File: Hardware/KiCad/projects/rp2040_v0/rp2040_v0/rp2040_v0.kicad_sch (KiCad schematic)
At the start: 52 parts, among them J1 Conn_01x03, J11 Conn_01x02, J12 Screw_Terminal_01x02, J2 Conn_01x02, J3 Conn_01x03, J5 USB_B_Micro, J8 Conn_01x03, J9 Conn_01x02, U1 W25Q128JVSIQTR, U2 AMS1117-3.3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

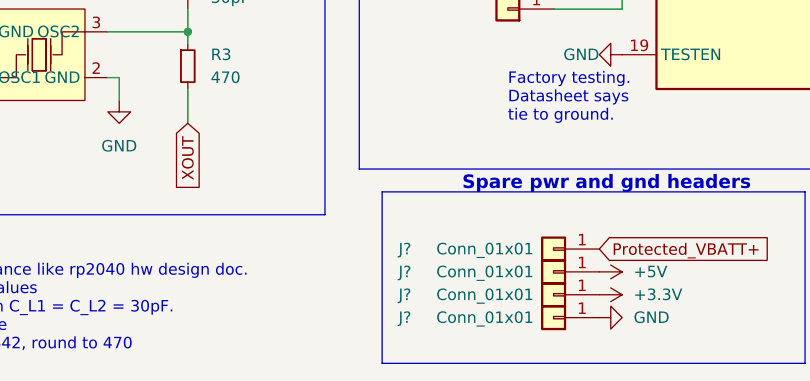
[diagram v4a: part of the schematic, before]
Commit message: Remove reaction wheel LDO. Add jumper to select power source.
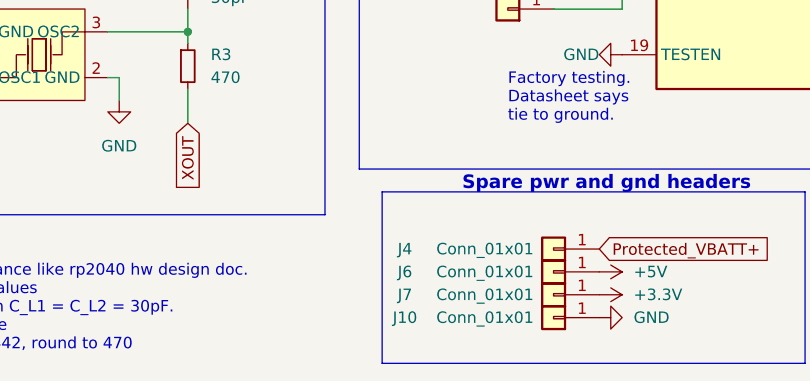
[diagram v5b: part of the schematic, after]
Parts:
- gave numbers to parts that had none: 4
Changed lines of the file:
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@@
   (symbol (lib_id "Connector_Generic:Conn_01x01") (at 110.49 189.23 180) (unit 1)
     (in_bom yes) (on_board yes)
-    (property "Reference" "J?" (id 0) (at 93.98 189.23 0))
+    (property "Reference" "J7" (id 0) (at 93.98 189.23 0))
     (property "Value" "Conn_01x01" (id 1) (at 102.87 189.23 0))
     (property "Footprint" "Connector_PinHeader_2.54mm:PinHeader_1x01_P2.54mm_Vertical" (id 2) (at 110.49 189.23 0)
@@
   (symbol (lib_id "Connector_Generic:Conn_01x01") (at 110.49 184.15 180) (unit 1)
     (in_bom yes) (on_board yes)
-    (property "Reference" "J?" (id 0) (at 93.98 184.15 0))
+    (property "Reference" "J4" (id 0) (at 93.98 184.15 0))
     (property "Value" "Conn_01x01" (id 1) (at 102.87 184.15 0))
     (property "Footprint" "Connector_PinHeader_2.54mm:PinHeader_1x01_P2.54mm_Vertical" (id 2) (at 110.49 184.15 0)
@@
   (symbol (lib_id "Connector_Generic:Conn_01x01") (at 110.49 186.69 180) (unit 1)
     (in_bom yes) (on_board yes)
-    (property "Reference" "J?" (id 0) (at 93.98 186.69 0))
+    (property "Reference" "J6" (id 0) (at 93.98 186.69 0))
     (property "Value" "Conn_01x01" (id 1) (at 102.87 186.69 0))
     (property "Footprint" "Connector_PinHeader_2.54mm:PinHeader_1x01_P2.54mm_Vertical" (id 2) (at 110.49 186.69 0)
@@
   (symbol (lib_id "Connector_Generic:Conn_01x01") (at 110.49 191.77 180) (unit 1)
     (in_bom yes) (on_board yes)
-    (property "Reference" "J?" (id 0) (at 93.98 191.77 0))
+    (property "Reference" "J10" (id 0) (at 93.98 191.77 0))
     (property "Value" "Conn_01x01" (id 1) (at 102.87 191.77 0))
     (property "Footprint" "Connector_PinHeader_2.54mm:PinHeader_1x01_P2.54mm_Vertical" (id 2) (at 110.49 191.77 0)
@@
       (reference "#FLG05") (unit 1) (value "PWR_FLAG") (footprint "")
     )
-    (path "/80e37a29-2645-40c2-ad1a-3b8bdd51b77d/ede4d486-c12c-47f9-9937-34a5c7182f83"
-      (reference "#FLG06") (unit 1) (value "PWR_FLAG") (footprint "")
-    )
     (path "/848a71b8-bab3-424a-a51e-99629cb440e3/b7521c9c-bf64-45b2-a3fb-89e8fba8c1f5"
       (reference "#FLG07") (unit 1) (value "PWR_FLAG") (footprint "")
@@
       (reference "#FLG08") (unit 1) (value "PWR_FLAG") (footprint "")
     )
-    (path "/80e37a29-2645-40c2-ad1a-3b8bdd51b77d/35089b51-702e-46a1-a9df-a3739d74f6c0"
-      (reference "#FLG0101") (unit 1) (value "PWR_FLAG") (footprint "")
-    )
     (path "/617f9643-808b-4ea3-942b-831275ec22c7"
       (reference "#PWR01") (unit 1) (value "GND") (footprint "")
@@
       (reference "#PWR065") (unit 1) (value "GND") (footprint "")
     )
-    (path "/848a71b8-bab3-424a-a51e-99629cb440e3/57f0a757-1548-4ffe-8cd3-6386ca83e54d"
-      (reference "#PWR070") (unit 1) (value "GND") (footprint "")
-    )
     (path "/848a71b8-bab3-424a-a51e-99629cb440e3/72340d32-b611-4acb-8287-9f496904fa54"
       (reference "#PWR071") (unit 1) (value "+3.3V") (footprint "")
@@
       (reference "#PWR0105") (unit 1) (value "+5V") (footprint "")
     )
+    (path "/848a71b8-bab3-424a-a51e-99629cb440e3/29d577bc-6eb3-4898-9657-27014c165883"
+      (reference "#PWR0106") (unit 1) (value "+5V") (footprint "")
+    )
     (path "/80e37a29-2645-40c2-ad1a-3b8bdd51b77d/f56621e1-0429-4070-aa37-c7f1ca7e72ef"
       (reference "BZ1") (unit 1) (value "Buzzer") (footprint "easyeda2kicad:BUZ-TH_BD9.0-P4.00-D0.6-FD")
@@
       (reference "C28") (unit 1) (value "10uF") (footprint "Capacitor_SMD:C_0805_2012Metric")
     )
-    (path "/848a71b8-bab3-424a-a51e-99629cb440e3/d051c7b0-d333-4fac-8ce2-62cecdfb9039"
-      (reference "C35") (unit 1) (value "10uF") (footprint "Capacitor_SMD:C_0805_2012Metric")
-    )
-    (path "/848a71b8-bab3-424a-a51e-99629cb440e3/ed6a7b12-8e4a-4c44-b186-747a7b75bac2"
-      (reference "C36") (unit 1) (value "10uF") (footprint "Capacitor_SMD:C_0805_2012Metric")
-    )
     (path "/848a71b8-bab3-424a-a51e-99629cb440e3/e64388e5-db0a-4e46-afd5-4bb8a4ef122e"
       (reference "C37") (unit 1) (value "DNP") (footprint "Capacitor_SMD:C_0603_1608Metric")
@@
       (reference "J3") (unit 1) (value "Conn_01x03") (footprint "Connector_PinHeader_2.54mm:PinHeader_1x03_P2.54mm_Vertical")
     )
+    (path "/8458783a-0147-49cd-9704-3db5c01e6fe3"
+      (reference "J4") (unit 1) (value "Conn_01x01") (footprint "Connector_PinHeader_2.54mm:PinHeader_1x01_P2.54mm_Vertical")
+    )
     (path "/3362f215-01d0-47bb-95bc-a3a8bc9d2087"
       (reference "J5") (unit 1) (value "USB_B_Micro") (footprint "easyeda2kicad:MICRO-USB-SMD_MICROXNJ")
     )
+    (path "/b5696ede-8606-4f2d-8627-4db654e29aac"
+      (reference "J6") (unit 1) (value "Conn_01x01") (footprint "Connector_PinHeader_2.54mm:PinHeader_1x01_P2.54mm_Vertical")
+    )
+    (path "/6137d0ac-1ed4-41ab-b93c-6083d09b10bf"
+      (reference "J7") (unit 1) (value "Conn_01x01") (footprint "Connector_PinHeader_2.54mm:PinHeader_1x01_P2.54mm_Vertical")
+    )
     (path "/5bc0b324-f551-4ef9-9acc-917626da077c"
       (reference "J8") (unit 1) (value "Conn_01x03") (footprint "Connector_PinHeader_2.54mm:PinHeader_1x03_P2.54mm_Vertical")
@@
       (reference "J9") (unit 1) (value "Conn_01x02") (footprint "Connector_PinHeader_2.54mm:PinHeader_1x02_P2.54mm_Vertical")
     )
+    (path "/bb4bc4f5-47f9-434a-ac80-d99731d08e26"
+      (reference "J10") (unit 1) (value "Conn_01x01") (footprint "Connector_PinHeader_2.54mm:PinHeader_1x01_P2.54mm_Vertical")
+    )
     (path "/bab6fd12-af94-4255-9b9f-edcfe4aeb46b"
       (reference "J11") (unit 1) (value "Conn_01x02") (footprint "Connector_PinHeader_2.54mm:PinHeader_1x02_P2.54mm_Vertical")
@@
       (reference "J15") (unit 1) (value "Conn_01x02") (footprint "Connector_PinHeader_2.54mm:PinHeader_1x02_P2.54mm_Vertical")
     )
+    (path "/848a71b8-bab3-424a-a51e-99629cb440e3/598a9772-81af-40cf-948c-759920cf0388"
+      (reference "J16") (unit 1) (value "Conn_01x03") (footprint "Connector_PinHeader_2.54mm:PinHeader_1x03_P2.54mm_Vertical")
+    )
     (path "/b2681fff-d31e-456f-82ce-345e7022a044/2b8dd97c-a36c-4c2e-9f43-cd4610ba40ca"
       (reference "J17") (unit 1) (value "Conn_01x03") (footprint "Connector_PinHeader_2.54mm:PinHeader_1x03_P2.54mm_Vertical")
@@
       (reference "J28") (unit 1) (value "Screw_Terminal_01x02") (footprint "easyeda2kicad:CONN-TH_XY301V-A-5.0-2P")
     )
-    (path "/6137d0ac-1ed4-41ab-b93c-6083d09b10bf"
-      (reference "J?") (unit 1) (value "Conn_01x01") (footprint "Connector_PinHeader_2.54mm:PinHeader_1x01_P2.54mm_Vertical")
-    )
-    (path "/8458783a-0147-49cd-9704-3db5c01e6fe3"
-      (reference "J?") (unit 1) (value "Conn_01x01") (footprint "Connector_PinHeader_2.54mm:PinHeader_1x01_P2.54mm_Vertical")
-    )
-    (path "/b5696ede-8606-4f2d-8627-4db654e29aac"
-      (reference "J?") (unit 1) (value "Conn_01x01") (footprint "Connector_PinHeader_2.54mm:PinHeader_1x01_P2.54mm_Vertical")
-    )
-    (path "/bb4bc4f5-47f9-434a-ac80-d99731d08e26"
-      (reference "J?") (unit 1) (value "Conn_01x01") (footprint "Connector_PinHeader_2.54mm:PinHeader_1x01_P2.54mm_Vertical")
-    )
     (path "/e648d3b1-eed1-4f79-8d45-25203286cbe0"
       (reference "LED1") (unit 1) (value "KT-0603R") (footprint "easyeda2kicad:LED0603-R-RD")
@@
       (reference "U8") (unit 1) (value "AMS1117-5.0") (footprint "Package_TO_SOT_SMD:SOT-223-3_TabPin2")
     )
-    (path "/848a71b8-bab3-424a-a51e-99629cb440e3/808ba4ae-b095-44f9-8cb6-43b798d7c843"
-      (reference "U11") (unit 1) (value "AMS1117-5.0") (footprint "Package_TO_SOT_SMD:SOT-223-3_TabPin2")
-    )
     (path "/848a71b8-bab3-424a-a51e-99629cb440e3/c89f0bc7-1ca5-4f75-9651-6accbac669a8"

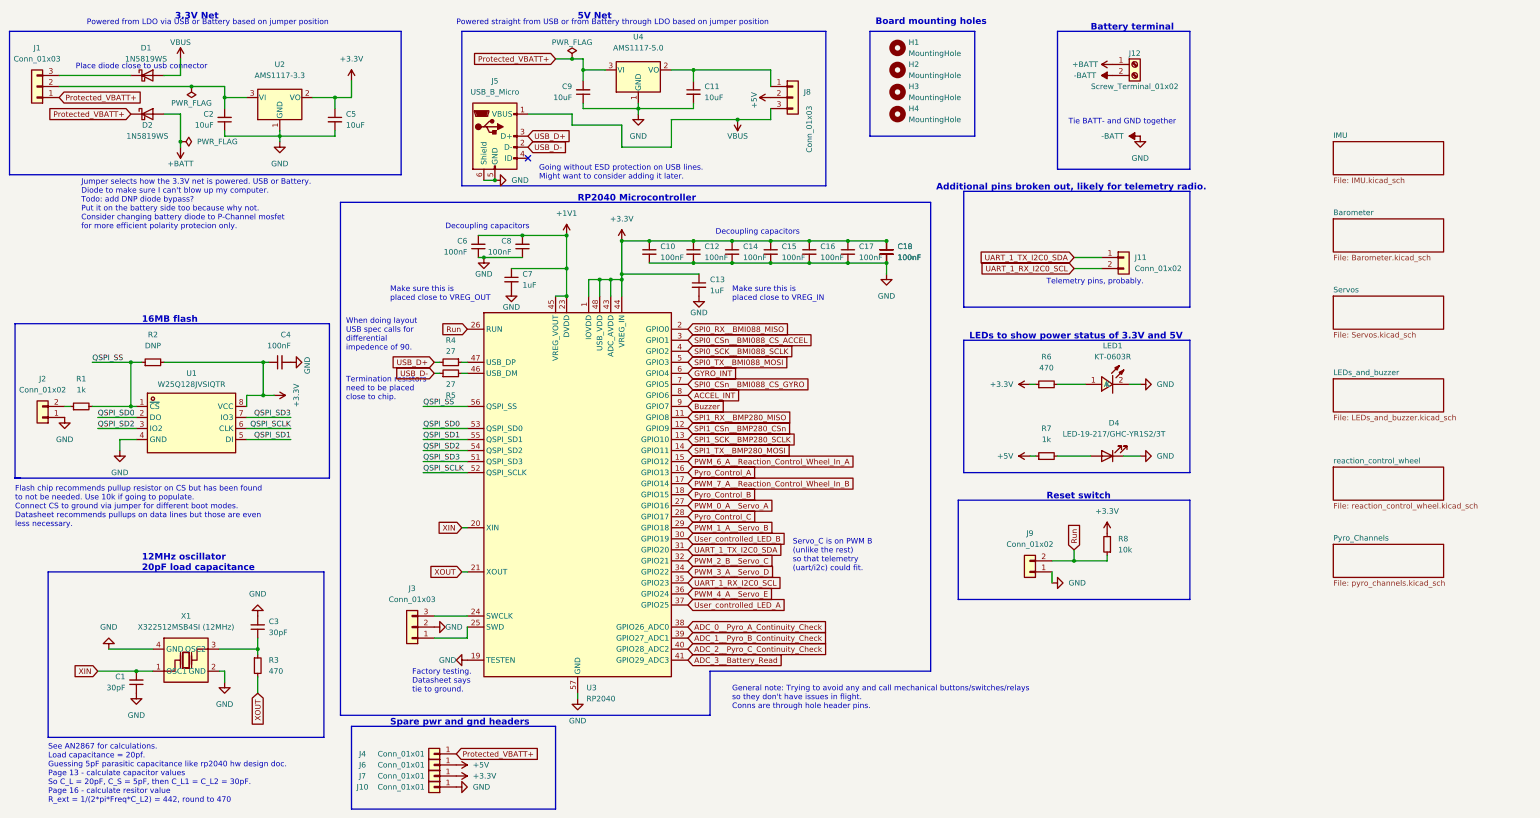
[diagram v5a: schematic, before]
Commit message: Delete and readd old components to appease the DRC
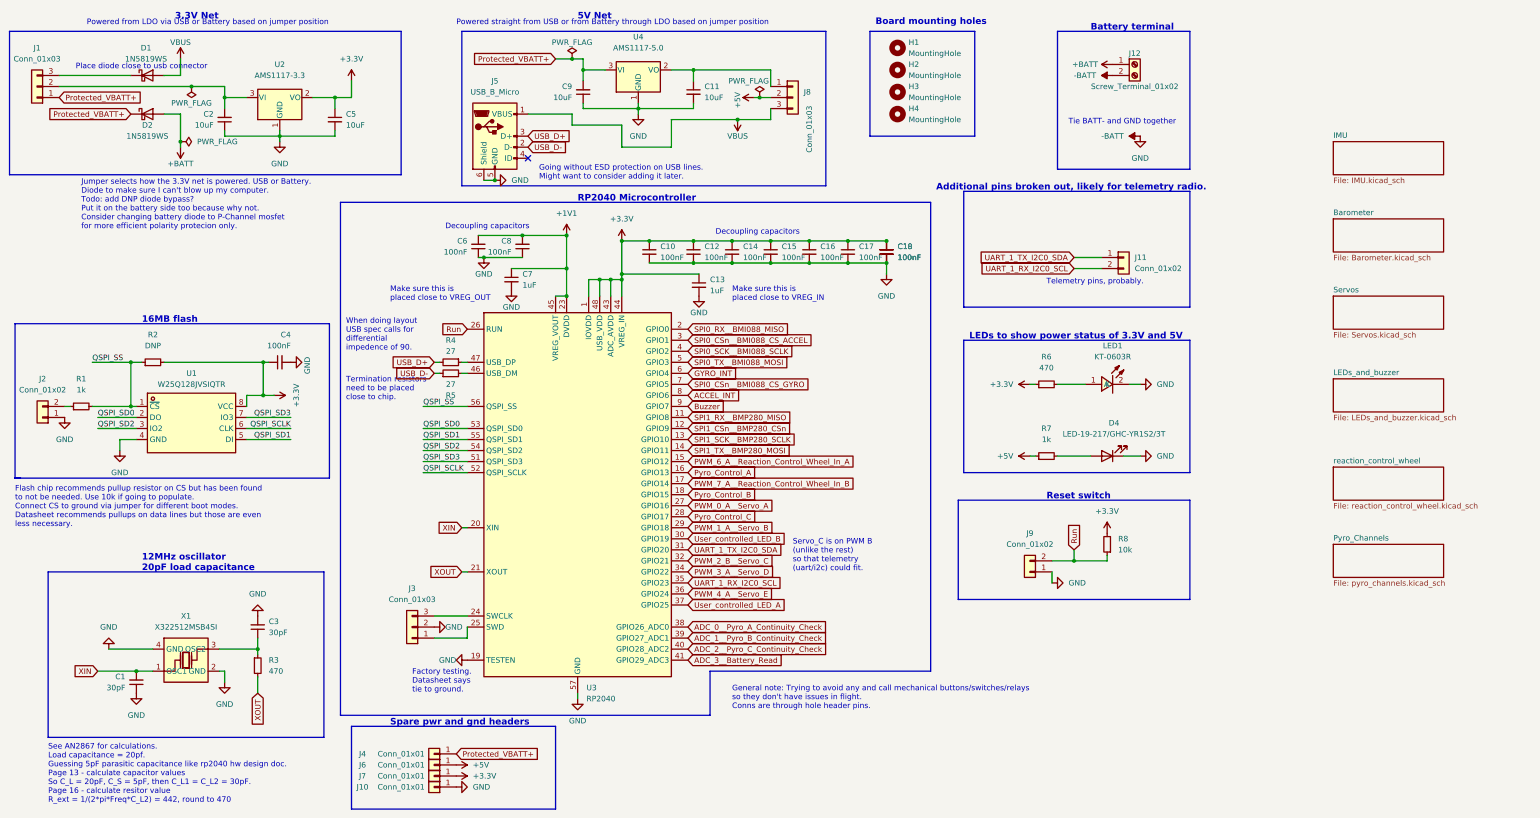
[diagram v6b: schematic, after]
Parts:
- removed U1: W25Q128JVSIQTR, easyeda2kicad:SOIC-8_L5.3-W5.3-P1.27-LS8.0-BL, symbol easyeda2kicad:W25Q128JVSIQTR
- removed X1: X322512MSB4SI (12MHz), easyeda2kicad:OSC-SMD_4P-L3.2-W2.5-BL, symbol easyeda2kicad:X322512MSB4SI
- added U1: W25Q128JVSIQTR, easyeda2kicad:SOIC-8_L5.3-W5.3-P1.27-LS8.0-BL, symbol easyeda2kicad_flight_computer:W25Q128JVSIQTR
- added X1: X322512MSB4SI, easyeda2kicad:OSC-SMD_4P-L3.2-W2.5-BL, symbol easyeda2kicad_flight_computer:X322512MSB4SI
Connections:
- net +3.3V: now also U1.8 (VCC)
- net -BATT: now also U1.4 (GND), X1.2 (GND), X1.4 (GND)
- net QSPI_SCLK: now also U1.6 (CLK)
- net QSPI_SD0: now also U1.2 (DO)
- net QSPI_SD1: now also U1.5 (DI)
- net QSPI_SD2: now also U1.3 (IO2)
- net QSPI_SD3: now also U1.7 (IO3)
- net QSPI_SS: now also U1.1 (~{CS})
- net XIN: now also X1.1 (OSC1)
- net at C3.1, R3.1: now also X1.3 (OSC2)

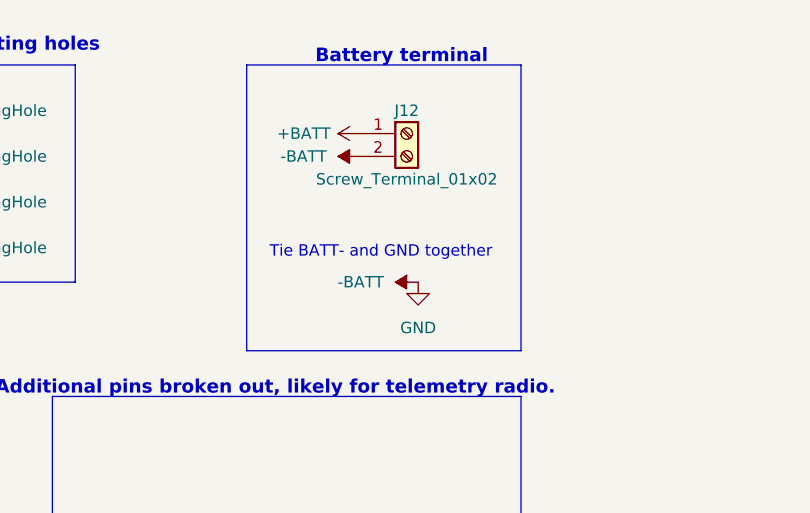
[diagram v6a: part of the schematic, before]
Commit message: Remove -Batt and just call it GND so it's less confusing in PCB
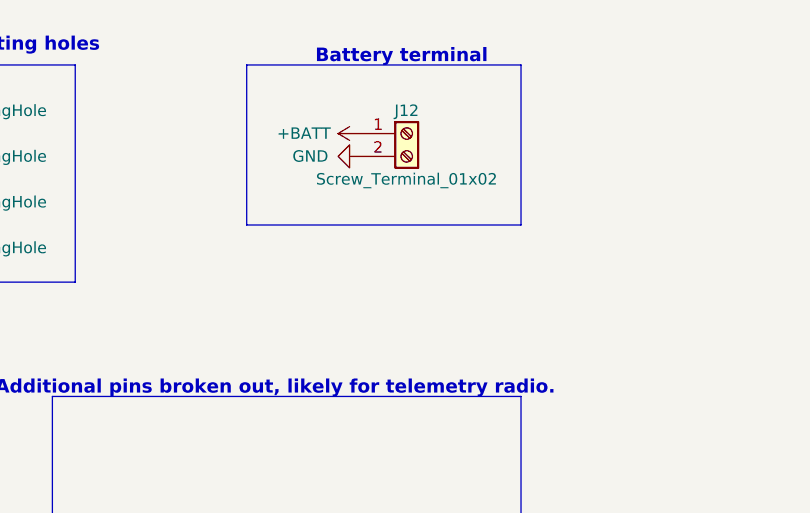
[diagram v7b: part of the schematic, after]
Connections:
- net -BATT renamed GND
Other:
- note removed: "Tie BATT- and GND together"
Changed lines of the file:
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@@
   )
   (no_connect (at 132.08 46.99))
-  (polyline (pts (xy 284.48 49.53) (xy 254 49.53))
+  (polyline (pts (xy 284.48 35.56) (xy 254 35.56))
     (stroke (width 0) (type default) (color 0 0 0 0))
   )
@@
     (stroke (width 0) (type default) (color 0 0 0 0))
   )
-  (polyline (pts (xy 284.48 17.78) (xy 284.48 49.53))
+  (polyline (pts (xy 284.48 17.78) (xy 284.48 35.56))
     (stroke (width 0) (type default) (color 0 0 0 0))
   )
@@
     (stroke (width 0) (type default) (color 0 0 0 0))
   )
-  (polyline (pts (xy 254 49.53) (xy 254 17.78))
+  (polyline (pts (xy 254 35.56) (xy 254 17.78))
     (stroke (width 0) (type default) (color 0 0 0 0))
   )
@@
   (text "See AN2867 for calculations.\nLoad capacitance = 20pf.\nGuessing 5pF parasitic capacitance like rp2040 hw design doc.\nPage 13 - calculate capacitor values\nSo C_L = 20pF, C_S = 5pF, then C_L1 = C_L2 = 30pF.\nPage 16 - calculate resitor value\nR_ext = 1/(2*pi*Freq*C_L2) = 442, round to 470"
     (at 21.59 195.58 0)
-    (effects (font (size 1.27 1.27)) (justify left bottom))
-  )
-  (text "Tie BATT- and GND together" (at 256.54 39.37 0)
     (effects (font (size 1.27 1.27)) (justify left bottom))
   )
@@
     (pin "3")
   )
-  (symbol (lib_id "power:-BATT") (at 273.05 41.91 90) (unit 1)
-    (in_bom yes) (on_board yes) (fields_autoplaced)
-    (property "Reference" "#PWR035" (id 0) (at 276.86 41.91 0)
-      (effects (font (size 1.27 1.27)) hide)
-    )
-    (property "Value" "-BATT" (id 1) (at 269.24 41.9099 90)
-      (effects (font (size 1.27 1.27)) (justify left))
-    )
-    (property "Footprint" "" (id 2) (at 273.05 41.91 0)
-      (effects (font (size 1.27 1.27)) hide)
-    )
-    (property "Datasheet" "" (id 3) (at 273.05 41.91 0)
-      (effects (font (size 1.27 1.27)) hide)
-    )
-    (pin "1")
-  )
   (symbol (lib_id "Mechanical:MountingHole") (at 217.17 31.75 0) (unit 1)
     (in_bom yes) (on_board yes) (fields_autoplaced)
@@
     )
     (property "Datasheet" "" (id 3) (at 273.05 99.06 0)
-      (effects (font (size 1.27 1.27)) hide)
-    )
-    (pin "1")
-  )
-  (symbol (lib_id "power:GND") (at 273.05 41.91 0) (unit 1)
-    (in_bom yes) (on_board yes) (fields_autoplaced)
-    (property "Reference" "#PWR036" (id 0) (at 273.05 48.26 0)
-      (effects (font (size 1.27 1.27)) hide)
-    )
-    (property "Value" "GND" (id 1) (at 273.05 46.99 0))
-    (property "Footprint" "" (id 2) (at 273.05 41.91 0)
-      (effects (font (size 1.27 1.27)) hide)
-    )
-    (property "Datasheet" "" (id 3) (at 273.05 41.91 0)
       (effects (font (size 1.27 1.27)) hide)
     )
@@
     )
     (property "Datasheet" "~" (id 3) (at 110.49 191.77 0)
-      (effects (font (size 1.27 1.27)) hide)
-    )
-    (pin "1")
-  )
-  (symbol (lib_id "power:-BATT") (at 266.7 27.94 90) (unit 1)
-    (in_bom yes) (on_board yes) (fields_autoplaced)
-    (property "Reference" "#PWR034" (id 0) (at 270.51 27.94 0)
-      (effects (font (size 1.27 1.27)) hide)
-    )
-    (property "Value" "-BATT" (id 1) (at 262.89 27.9399 90)
-      (effects (font (size 1.27 1.27)) (justify left))
-    )
-    (property "Footprint" "" (id 2) (at 266.7 27.94 0)
-      (effects (font (size 1.27 1.27)) hide)
-    )
-    (property "Datasheet" "" (id 3) (at 266.7 27.94 0)
       (effects (font (size 1.27 1.27)) hide)
     )
@@
     (pin "2")
   )
+  (symbol (lib_id "power:GND") (at 266.7 27.94 270) (unit 1)
+    (in_bom yes) (on_board yes)
+    (property "Reference" "#PWR?" (id 0) (at 260.35 27.94 0)
+      (effects (font (size 1.27 1.27)) hide)
+    )
+    (property "Value" "GND" (id 1) (at 259.08 27.94 90)
+      (effects (font (size 1.27 1.27)) (justify left))
+    )
+    (property "Footprint" "" (id 2) (at 266.7 27.94 0)
+      (effects (font (size 1.27 1.27)) hide)
+    )
+    (property "Datasheet" "" (id 3) (at 266.7 27.94 0)
+      (effects (font (size 1.27 1.27)) hide)
+    )
+    (pin "1")
+  )
   (symbol (lib_id "power:+3.3V") (at 153.67 66.04 0) (unit 1)
     (in_bom yes) (on_board yes) (fields_autoplaced)
@@
       (reference "#PWR033") (unit 1) (value "+BATT") (footprint "")
     )
-    (path "/c0e98022-4f5a-44ce-ada0-43248a23d7b7"
-      (reference "#PWR034") (unit 1) (value "-BATT") (footprint "")
-    )
-    (path "/8bdc48e9-5ba0-4911-9a6f-265dd1ef1573"
-      (reference "#PWR035") (unit 1) (value "-BATT") (footprint "")
-    )
-    (path "/a8f258f4-6525-45ce-bc5c-e39151263ed7"
-      (reference "#PWR036") (unit 1) (value "GND") (footprint "")
-    )
     (path "/a5c7d8c9-ec38-426f-a7ea-686ab7c646ff"
       (reference "#PWR037") (unit 1) (value "GND") (footprint "")
@@
       (reference "#PWR0106") (unit 1) (value "+5V") (footprint "")
     )
+    (path "/fb79d012-1007-418b-b24e-637df639e8d0"
+      (reference "#PWR?") (unit 1) (value "GND") (footprint "")
+    )
     (path "/80e37a29-2645-40c2-ad1a-3b8bdd51b77d/f56621e1-0429-4070-aa37-c7f1ca7e72ef"
